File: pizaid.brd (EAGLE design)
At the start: 65 x 56 mm, 40 parts

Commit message: added gerber
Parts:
- R4: device rcl:0204/7 -> rcl:0207/10
- moved R4 1.25 mm to (75.5, 49.7)
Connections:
- removed net B7: U$8.P$16
- net 5V0@2: now also U$8.P$15, U$8.P$16
- net B2: now also PCB1.17
- net B3: now also PCB1.19
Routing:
- net GND: track 337.2 -> 323.5 mm
- net 5V0@2: track 91.2 -> 96.2 mm
- net B3: track 0.00 -> 2.54 mm
- net B2: track 34.0 -> 36.5 mm
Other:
- board text added: "rev. 1 14/10/01"
- board text removed: "rev. 1 2014/10/01"
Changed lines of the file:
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@@
 <wire x1="58.75" y1="40.5" x2="64.25" y2="35" width="0.1" layer="42"/>
 <wire x1="64.25" y1="35" x2="64.25" y2="33.75" width="0.1" layer="42"/>
-<wire x1="26" y1="42.5" x2="26" y2="30" width="0.1" layer="42"/>
+<wire x1="26" y1="45.25" x2="26" y2="30" width="0.1" layer="42"/>
 <wire x1="26" y1="30" x2="26" y2="17.5" width="0.1" layer="42"/>
-<wire x1="26" y1="17.5" x2="32" y2="11.5" width="0.1" layer="42"/>
-<wire x1="32" y1="11.5" x2="32" y2="4.25" width="0.1" layer="42"/>
-<wire x1="32" y1="4.25" x2="32" y2="11.5" width="0.1" layer="41"/>
-<wire x1="32" y1="11.5" x2="26" y2="17.5" width="0.1" layer="41"/>
 <wire x1="26" y1="17.5" x2="26" y2="30" width="0.1" layer="41"/>
-<wire x1="26" y1="30" x2="26" y2="42.5" width="0.1" layer="41"/>
+<wire x1="26" y1="30" x2="26" y2="45.25" width="0.1" layer="41"/>
 <wire x1="26" y1="30" x2="35.5" y2="30" width="0.1" layer="42"/>
 <wire x1="35.5" y1="30" x2="40" y2="34.5" width="0.1" layer="42"/>
@@
 <wire x1="25" y1="7" x2="28" y2="4" width="0.1" layer="20" curve="90"/>
 <text x="51.25" y="54.25" size="1.778" layer="21">Pizaid battery manager</text>
-<text x="51.25" y="51.75" size="1.778" layer="21">rev. 1 2014/10/01</text>
+<text x="51.25" y="51.75" size="1.778" layer="21">rev. 1 14/10/01</text>
+<wire x1="31.5" y1="45.25" x2="26" y2="45.25" width="0.1" layer="41"/>
+<wire x1="31.5" y1="45.25" x2="26" y2="45.25" width="0.1" layer="42"/>
 </plain>
 <attributes>
@@
 <attribute name="VALUE" x="78.865" y="21.345" size="1.27" layer="27"/>
 </element>
-<element name="R4" library="rcl" package="0204/7" value="0.2" x="76.77" y="49.6625" smashed="yes" rot="R180">
-<attribute name="NAME" x="79.31" y="48.3671" size="0.9906" layer="25" ratio="10" rot="R180"/>
-<attribute name="VALUE" x="75.6044" y="51.1049" size="0.9906" layer="27" ratio="10"/>
+<element name="R4" library="rcl" package="0207/10" value="0.2" x="75.52" y="49.6625" smashed="yes" rot="R180">
+<attribute name="NAME" x="78.06" y="48.3671" size="0.9906" layer="25" ratio="10" rot="R180"/>
+<attribute name="VALUE" x="74.3544" y="51.1049" size="0.9906" layer="27" ratio="10"/>
 </element>
 <element name="R5" library="rcl" package="R0603" value="24" x="84" y="49" smashed="yes">
@@
 </element>
 <element name="L1" library="rcl" package="L5650M" value="33u" x="73.46" y="43.9475" smashed="yes" rot="R270">
-<attribute name="NAME" x="66.3975" y="48.885" size="1.27" layer="25"/>
-<attribute name="VALUE" x="68.6475" y="49.015" size="1.27" layer="27"/>
+<attribute name="NAME" x="66.1475" y="49.635" size="1.27" layer="25"/>
+<attribute name="VALUE" x="66.1475" y="48.015" size="1.27" layer="27"/>
 </element>
 <element name="L2" library="rcl" package="L5650M" value="33u" x="67.11" y="43.9475" smashed="yes" rot="R90">
-<attribute name="NAME" x="59.7925" y="48.815" size="1.27" layer="25"/>
-<attribute name="VALUE" x="62.5425" y="48.945" size="1.27" layer="27"/>
+<attribute name="NAME" x="62.5425" y="49.565" size="1.27" layer="25"/>
+<attribute name="VALUE" x="62.5425" y="47.945" size="1.27" layer="27"/>
 </element>
 <element name="U$2" library="pizaid" package="SOD-123FL" value="SS2040FL" x="70.285" y="35.0575" smashed="yes" rot="R180">
@@
 <contactref element="U$10" pad="P$2"/>
 <wire x1="80.575" y1="46.4875" x2="80.575" y2="49.1575" width="2" layer="1"/>
-<wire x1="80.575" y1="49.1575" x2="80.58" y2="49.6625" width="2" layer="1"/>
+<wire x1="80.575" y1="49.1575" x2="80.6" y2="49.6625" width="2" layer="1"/>
 <wire x1="80.575" y1="46.4875" x2="80.575" y2="42.1875" width="2" layer="1"/>
 <wire x1="80.575" y1="42.1875" x2="80.575" y2="36.5625" width="2" layer="1"/>
@@
 <wire x1="37.1875" y1="57.1875" x2="77.1875" y2="57.1875" width="2" layer="1"/>
 <wire x1="77.1875" y1="57.1875" x2="80.58" y2="53.795" width="2" layer="1"/>
-<wire x1="80.58" y1="49.6625" x2="80.58" y2="53.795" width="2" layer="1"/>
+<wire x1="80.6" y1="49.6625" x2="80.58" y2="53.795" width="2" layer="1"/>
 <wire x1="44.2975" y1="39.105" x2="44.38" y2="39.1875" width="0.6" layer="1"/>
 <wire x1="44.38" y1="39.1875" x2="45.4375" y2="39.1875" width="0.6" layer="1"/>
@@
 <wire x1="44.795" y1="15.125" x2="42.265" y2="15.125" width="0.5" layer="16"/>
 <wire x1="40.99" y1="13.85" x2="42.265" y2="15.125" width="0.5" layer="16"/>
-<wire x1="46.07" y1="13.85" x2="47.345" y2="15.125" width="0.5" layer="16"/>
-<wire x1="58.77" y1="13.85" x2="57.495" y2="15.125" width="0.5" layer="16"/>
-<wire x1="57.495" y1="15.125" x2="47.345" y2="15.125" width="0.5" layer="16"/>
 <wire x1="58.77" y1="6.23" x2="60.05" y2="7.51" width="0.5" layer="16"/>
 <wire x1="58.77" y1="13.85" x2="60.05" y2="12.57" width="0.5" layer="16"/>
@@
 <via x="60.75" y="56.5" extent="1-16" drill="0.6"/>
 <via x="79.25" y="53.5" extent="1-16" drill="0.6"/>
-<wire x1="80.58" y1="53.795" x2="79.25" y2="53.5" width="0" layer="19" extent="1-1"/>
-<wire x1="28.5" y1="7.5" x2="33.37" y2="8.77" width="0" layer="19" extent="1-1"/>
 </signal>
 <signal name="VCC">
@@
 <wire x1="67.11" y1="46.4475" x2="67.11" y2="48.0475" width="2" layer="1"/>
 <wire x1="67.11" y1="48.0475" x2="68.725" y2="49.6625" width="2" layer="1"/>
-<wire x1="72.96" y1="49.6625" x2="68.725" y2="49.6625" width="2" layer="1"/>
-<wire x1="72.96" y1="49.6625" x2="72.96" y2="51.8525" width="0.6" layer="1"/>
-<wire x1="72.96" y1="51.8525" x2="72.9375" y2="51.875" width="0.6" layer="1"/>
-<via x="72.9375" y="51.875" extent="1-16" drill="0.8" diameter="1.4"/>
-<wire x1="72.9375" y1="51.875" x2="83.3125" y2="51.875" width="0.6" layer="16"/>
+<wire x1="70.44" y1="49.6625" x2="68.725" y2="49.6625" width="2" layer="1"/>
+<wire x1="70.44" y1="49.6625" x2="70.46" y2="51.6025" width="0.6" layer="1"/>
+<wire x1="70.46" y1="51.6025" x2="70.4375" y2="51.875" width="0.6" layer="1"/>
+<via x="70.4375" y="51.875" extent="1-16" drill="0.8" diameter="1.4"/>
+<wire x1="70.4375" y1="51.875" x2="83.3125" y2="51.875" width="0.6" layer="16"/>
 <via x="83.3125" y="51.875" extent="1-16" drill="0.8" diameter="1.4"/>
 <wire x1="83.15" y1="49" x2="83.15" y2="51.7125" width="0.6" layer="1"/>
@@
 <wire x1="77.8125" y1="10" x2="76.875" y2="10.9375" width="0.6" layer="16"/>
 <wire x1="76.875" y1="10.9375" x2="69.6375" y2="10.9375" width="0.6" layer="16"/>
-<wire x1="67.1875" y1="16.25" x2="39.0625" y2="16.25" width="0.6" layer="16"/>
+<wire x1="67.1875" y1="16.25" x2="49" y2="16.25" width="0.6" layer="16"/>
+<wire x1="48.61" y1="16.25" x2="39.0625" y2="16.25" width="0.6" layer="16"/>
 <wire x1="39.0625" y1="16.25" x2="36.25" y2="19.0625" width="0.6" layer="16"/>
 <wire x1="36.25" y1="19.0625" x2="36.25" y2="23.4375" width="0.6" layer="16"/>
@@
 <wire x1="68.725" y1="11.85" x2="68.725" y2="14.7125" width="0.6" layer="16"/>
 <wire x1="68.725" y1="14.7125" x2="67.1875" y2="16.25" width="0.6" layer="16"/>
+<contactref element="U$8" pad="P$15"/>
+<contactref element="U$8" pad="P$16"/>
+<wire x1="48.61" y1="11.31" x2="48.61" y2="13.85" width="0.6" layer="16"/>
+<wire x1="48.61" y1="13.85" x2="48.61" y2="16.25" width="0.6" layer="16"/>
+<wire x1="48.61" y1="16.25" x2="49" y2="16.25" width="0.6" layer="16"/>
 <wire x1="39.9625" y1="22.89" x2="40" y2="24.0625" width="0" layer="19" extent="1-1"/>
 </signal>
@@
 <wire x1="83" y1="13" x2="81.85" y2="13" width="0.6" layer="1"/>
 <wire x1="71.15" y1="13" x2="70" y2="13" width="0.5" layer="1"/>
+<contactref element="PCB1" pad="17"/>
+<wire x1="61.31" y1="8.77" x2="61.31" y2="11.31" width="0.5" layer="1"/>
 </signal>
 <signal name="B3">
 <contactref element="U$8" pad="P$8"/>
+<contactref element="PCB1" pad="19"/>
+<wire x1="58.77" y1="8.77" x2="58.77" y2="11.31" width="0.5" layer="16"/>
 </signal>
 <signal name="B6">
 <contactref element="U$8" pad="P$14"/>
 </signal>
-<signal name="B7">
-<contactref element="U$8" pad="P$16"/>
-</signal>
 <signal name="GIRD">

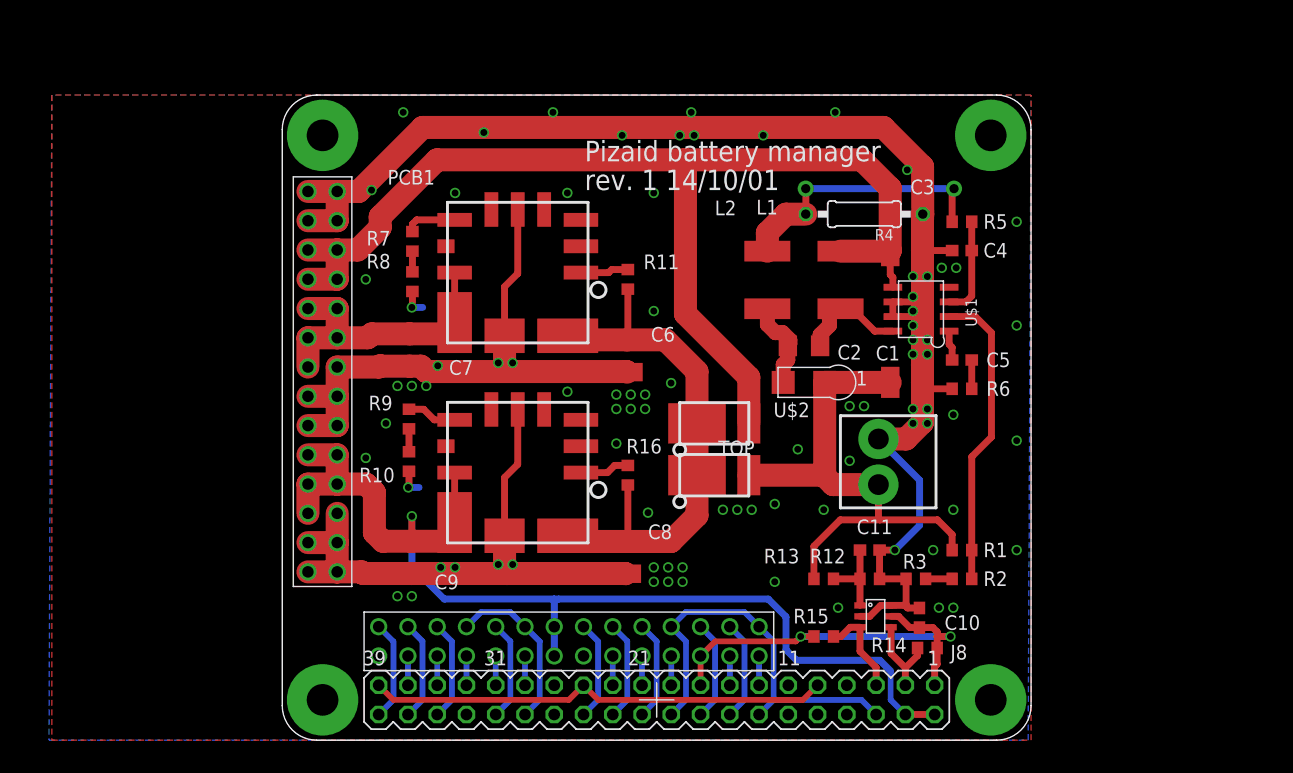
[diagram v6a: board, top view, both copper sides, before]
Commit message: modified battery board to output 12V
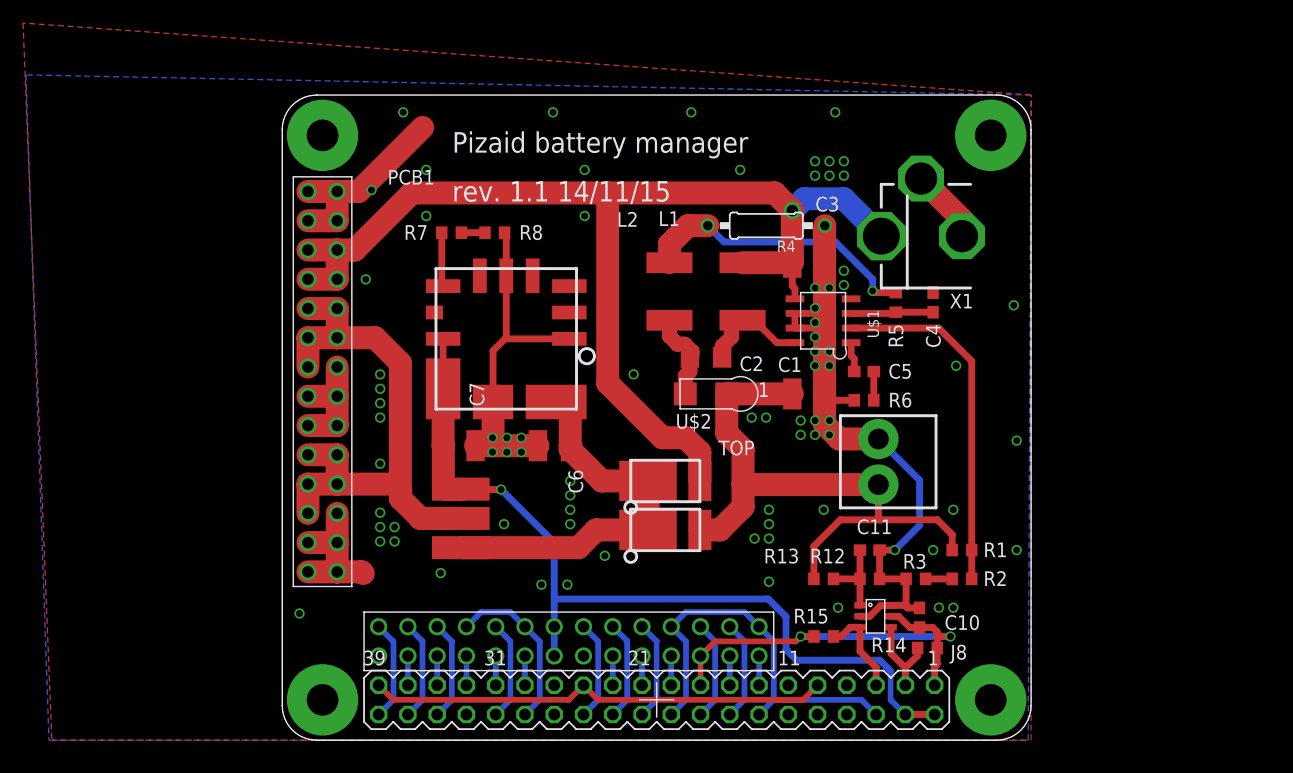
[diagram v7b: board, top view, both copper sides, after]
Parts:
- removed C8: 22u25V, rcl:C3225
- removed C9: 22u16V, rcl:C3225
- removed R10: 330, rcl:R0603
- removed R11, R16: 10k, rcl:R0603
- removed R9: 1k, rcl:R0603
- removed U$7: OKL-T/6, pizaid:OKL-T/6
- added U$11: SELECT_PAD, pizaid:SELECT_PAD
- added X1: DCJACK-MJ179P-R, kamiki-dcjack:MJ-179P-R
- moved C6 10.0 mm to (48.6, 29.6), turned to 180 degrees
- moved C7 9.36 mm to (40.4, 29.6), turned to 0 degrees
- moved R5 9.06 mm to (78.2, 42.0), turned to 270 degrees
- moved C1 8.56 mm to (70.7, 34.1)
- moved C2 8.56 mm to (61.8, 37.2)
- moved C3 8.56 mm to (70.7, 45.5)
- moved C5 8.56 mm to (75.5, 36.0)
- moved L1 8.56 mm to (65.0, 42.9)
- moved L2 8.56 mm to (58.6, 42.9)
- moved R4 8.56 mm to (67.0, 48.7)
- moved R6 8.56 mm to (75.5, 33.5)
- moved U$1 8.56 mm to (71.9, 40.4)
- moved U$2 8.56 mm to (61.8, 34.1)
- moved R8 8.32 mm to (43.5, 48.0), turned to 0 degrees
- moved U$5 6.56 mm to (58.2, 26.5)
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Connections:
- removed net JNET: C7.1, U$3.P$10, U$3.P$11, U$3.P$12, U$3.P$13, U$3.P$9, U$6.P$4, U$6.P$5
- removed net N$12: R16.1, U$7.P$1
- removed net N$14: R9.1, U$7.P$6
- removed net N$15: R10.1, R9.2
- removed net N$8: R11.1, U$6.P$1
- new net N$30: U$11.P$2, U$3.P$10, U$3.P$11, U$3.P$12, U$3.P$13, U$3.P$19, U$3.P$20, U$3.P$21, U$3.P$22, U$3.P$23, U$3.P$9
- net 5V0@2: now also C7.1, U$11.P$3, U$6.P$4, U$6.P$5; no longer C9.1, U$3.P$19, U$3.P$20, U$3.P$21, U$3.P$22, U$3.P$23, U$7.P$4, U$7.P$5
- net GIRD: now also U$11.P$1; no longer C8.1, R11.2, R16.2, U$7.P$2
- net GND: now also U$6.P$1, X1.2, X1.3; no longer C8.2, C9.2, R10.2, U$7.P$3, U$7.P$7
- net VCC: now also X1.1
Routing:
- net GND: track 323.5 -> 224.3 mm, vias 84 -> 79
- net N$30: track 0.00 -> 50.1 mm
- net JNET: track 26.1 -> 0.00 mm
- net 5V0@2: track 96.2 -> 74.6 mm
- net GIRD: track 46.8 -> 34.3 mm
- net N$3: track 46.2 -> 53.2 mm
- net N$14: track 4.34 -> 0.00 mm
- net N$12: track 4.34 -> 0.00 mm
- net N$10: track 26.3 -> 30.6 mm
- net N$8: track 4.19 -> 0.00 mm
- net VCC: track 98.6 -> 100.9 mm, vias 0 -> 1
- net N$15: track 1.99 -> 0.00 mm
- net N$5: track 8.63 -> 7.27 mm
- net N$4: track 23.6 -> 24.9 mm, vias 2 -> 1
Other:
- board text added: "rev. 1.1 14/11/15"
- board text removed: "rev. 1 14/10/01"
